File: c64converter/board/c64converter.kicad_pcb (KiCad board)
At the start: 2 copper layers, 53.3 x 27.9 mm, 38 parts, among them P1 LUMA, P2 LUMA_GND, P3 CHROMA, P4 CHROMA_GND, P5 VIN, P6 VIN_GND, P7 GPIO2, U1 APE8865Y5-30-HF-3, U2 AD9283BRSZ-80, U3 AD9283BRSZ-80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

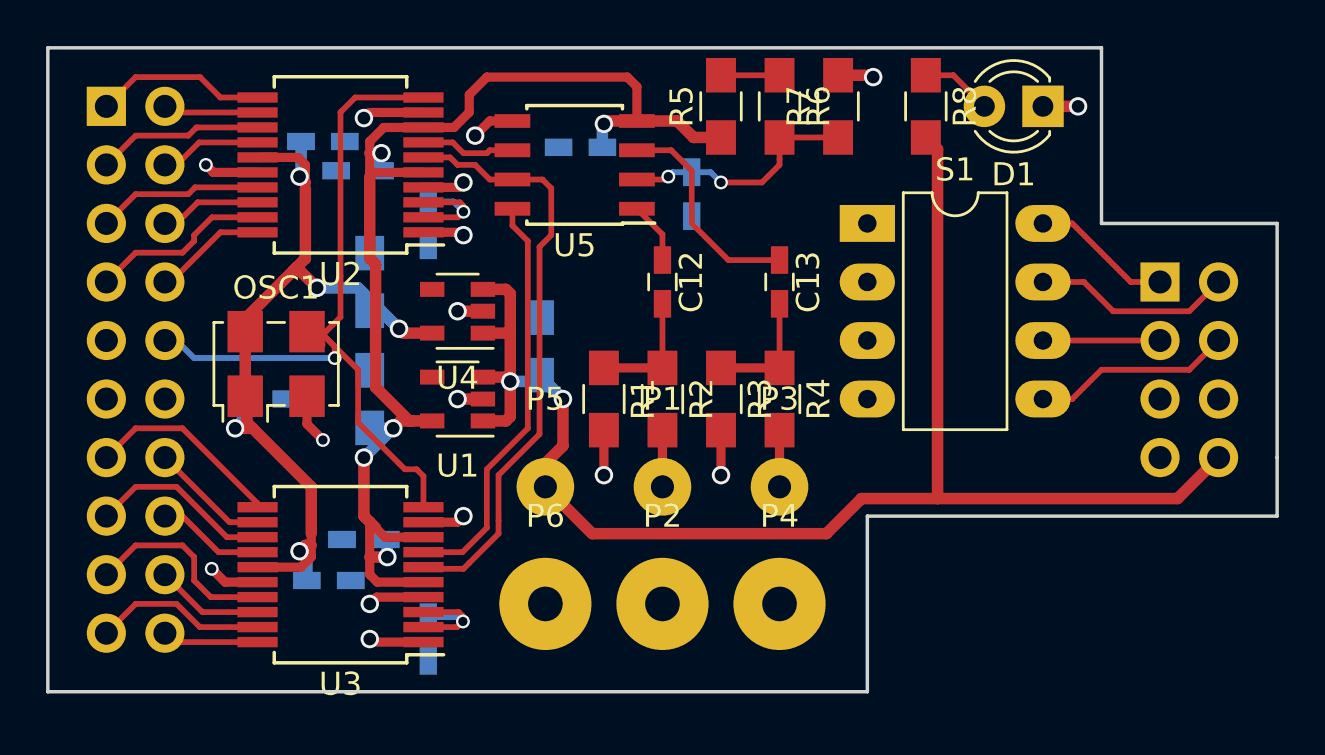
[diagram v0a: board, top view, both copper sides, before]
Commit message: Finished c64converter layout and gerber files
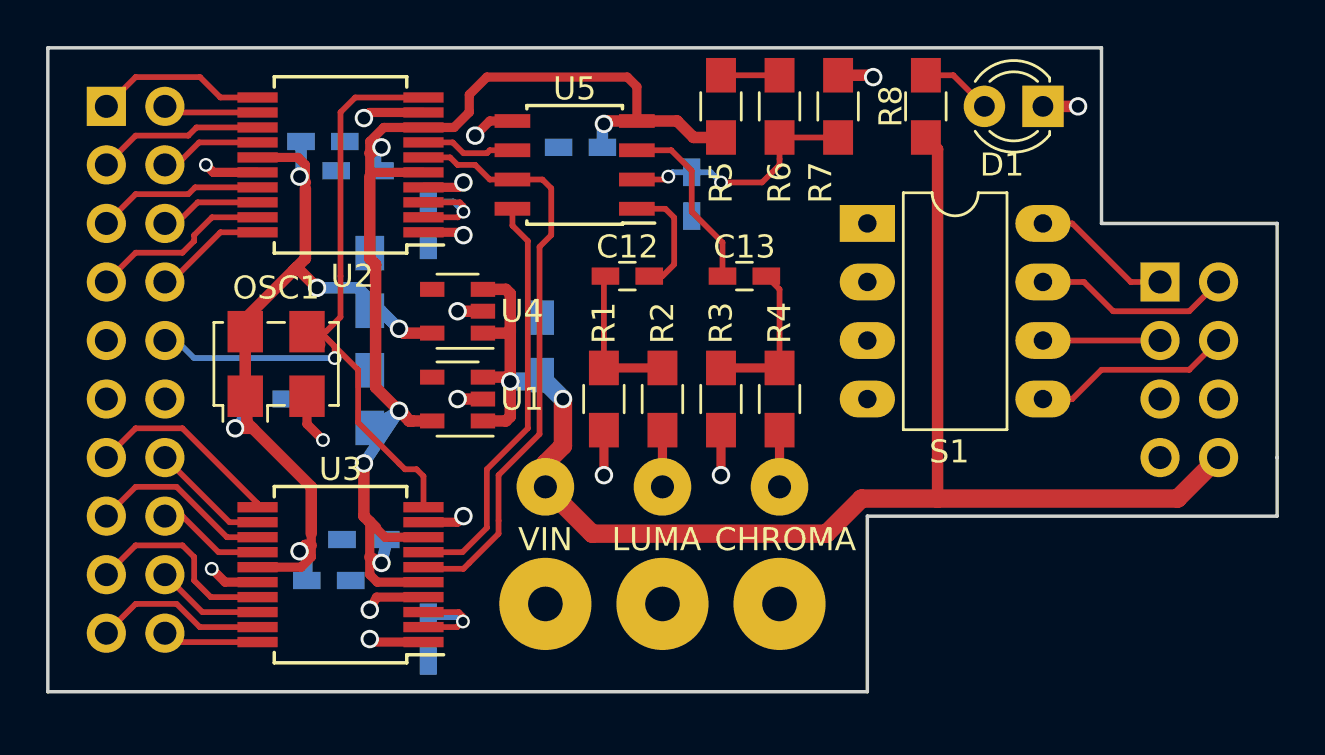
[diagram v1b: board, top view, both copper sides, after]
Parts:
- moved C12 1.55 mm to (139.4, 98.8), turned to 180 degrees
- moved C13 1.55 mm to (144.5, 98.8), turned to 0 degrees
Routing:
- net Net-(C12-Pad1): track 2.68 -> 5.10 mm
- net Net-(C13-Pad1): track 9.50 -> 7.87 mm
- net /3.0V: track 54.5 -> 55.9 mm
- net Net-(C13-Pad2): track 5.32 -> 6.76 mm
- net Net-(C12-Pad2): track 5.32 -> 6.55 mm
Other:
- board text added: "C64converter github.com /c0pperdragon /A-VideoBoard"
- board text added: "CHROMA"
- board text added: "LUMA"
- board text added: "VIN"
